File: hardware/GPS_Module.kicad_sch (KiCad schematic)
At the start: 10 parts, among them J3 Conn_01x04_Pin, J4 Conn_01x04_Pin, U6 SAM-M8Q

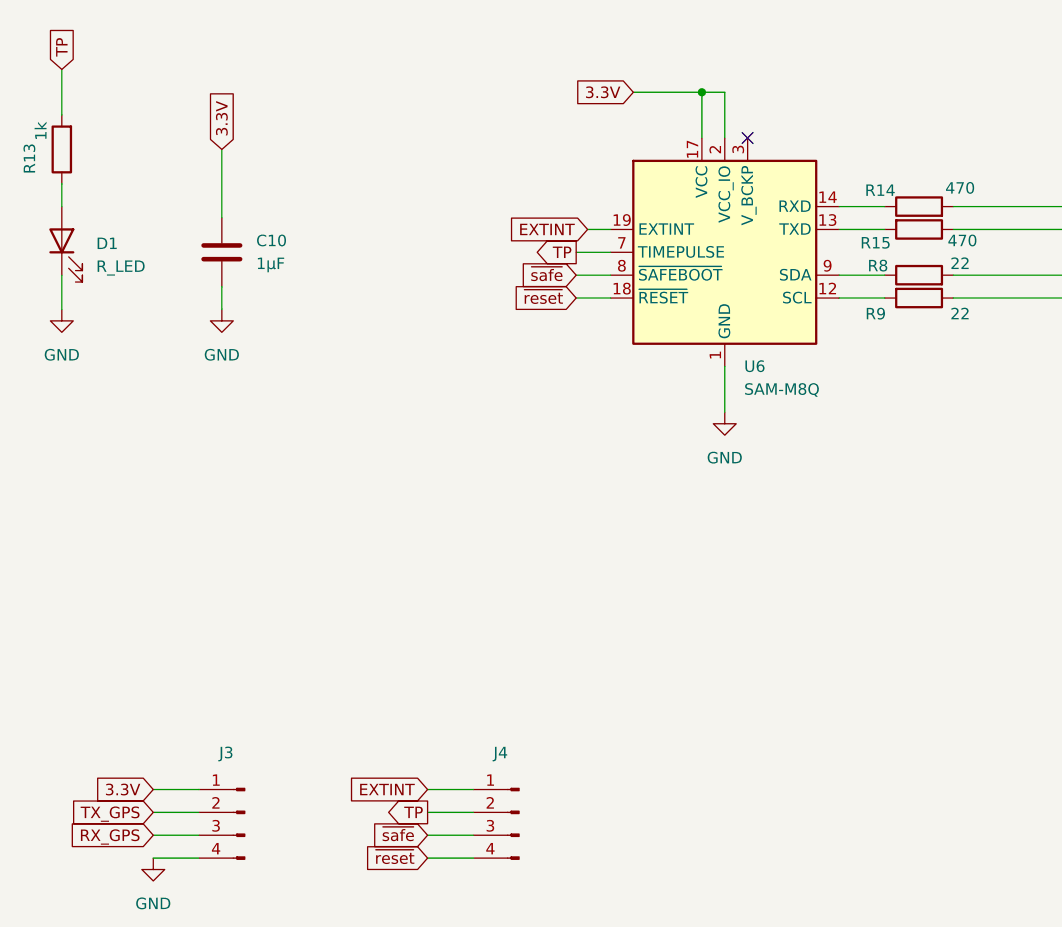
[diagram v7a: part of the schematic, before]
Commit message: Fix schematic components annotations
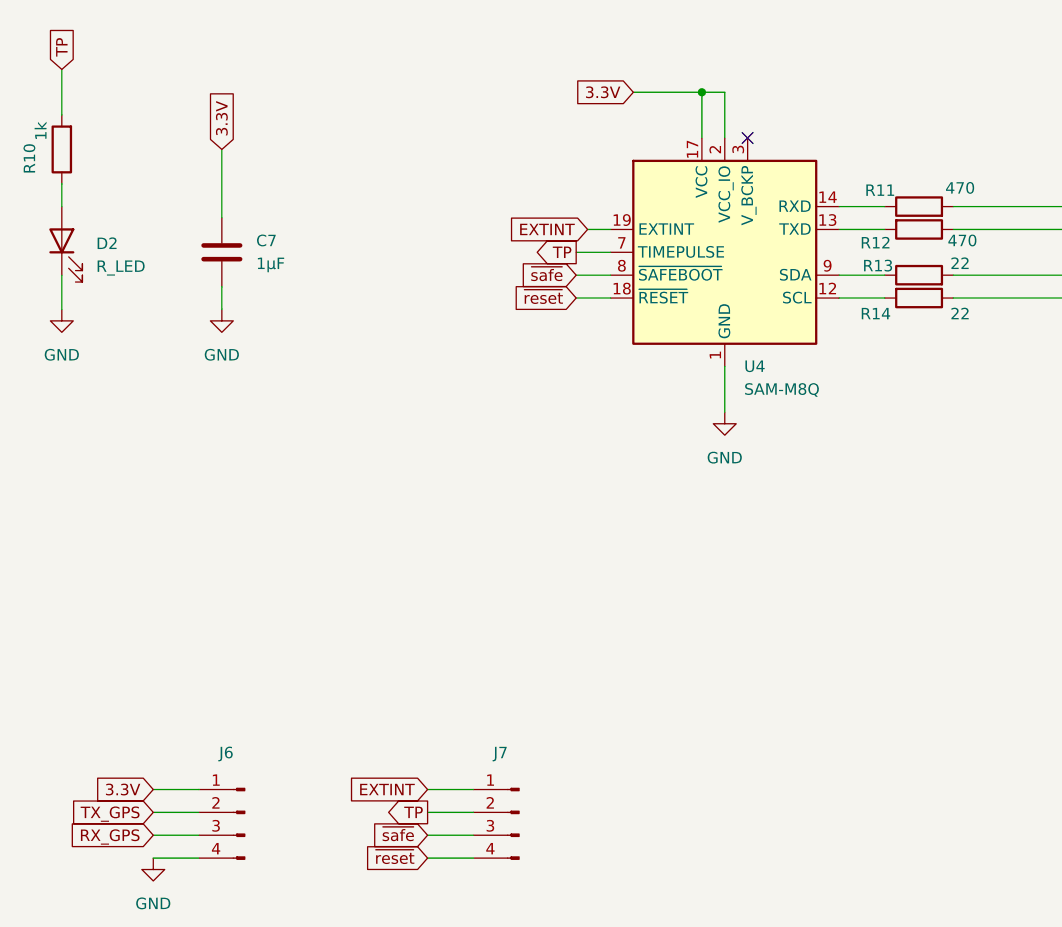
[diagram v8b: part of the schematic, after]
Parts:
- renumbered C10 to C7, D1 to D2, J3 to J6, J4 to J7, R13 to R10, R14 to R11, R15 to R12, R8 to R13, R9 to R14, U6 to U4
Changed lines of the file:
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@@
 		(on_board yes)
 		(dnp no)
-		(property "Reference" "R14"
+		(property "Reference" "R11"
 			(at 169.672 75.692 90)
 			(effects
@@
 			(project "GOG"
 				(path "/5b969f6e-a36e-432b-8f00-b2d6a515a877/86749ea3-b799-4cf0-94d1-46de6ccb32b0"
-					(reference "R14")
+					(reference "R11")
 					(unit 1)
 				)
@@
 		(dnp no)
 		(fields_autoplaced yes)
-		(property "Reference" "#PWR020"
+		(property "Reference" "#PWR019"
 			(at 88.9 156.21 0)
 			(effects
@@
 			(project "GOG"
 				(path "/5b969f6e-a36e-432b-8f00-b2d6a515a877/86749ea3-b799-4cf0-94d1-46de6ccb32b0"
-					(reference "#PWR020")
+					(reference "#PWR019")
 					(unit 1)
 				)
@@
 		(on_board yes)
 		(dnp no)
-		(property "Reference" "R9"
+		(property "Reference" "R14"
 			(at 169.164 89.408 90)
 			(effects
@@
 			(project "GOG"
 				(path "/5b969f6e-a36e-432b-8f00-b2d6a515a877/86749ea3-b799-4cf0-94d1-46de6ccb32b0"
-					(reference "R9")
+					(reference "R14")
 					(unit 1)
 				)
@@
 		(on_board yes)
 		(dnp no)
-		(property "Reference" "R15"
+		(property "Reference" "R12"
 			(at 169.164 81.534 90)
 			(effects
@@
 			(project "GOG"
 				(path "/5b969f6e-a36e-432b-8f00-b2d6a515a877/86749ea3-b799-4cf0-94d1-46de6ccb32b0"
-					(reference "R15")
+					(reference "R12")
 					(unit 1)
 				)
@@
 		(on_board yes)
 		(dnp no)
-		(property "Reference" "R13"
+		(property "Reference" "R10"
 			(at 75.184 72.136 90)
 			(effects
@@
 			(project "GOG"
 				(path "/5b969f6e-a36e-432b-8f00-b2d6a515a877/86749ea3-b799-4cf0-94d1-46de6ccb32b0"
-					(reference "R13")
+					(reference "R10")
 					(unit 1)
 				)
@@
 		(on_board yes)
 		(dnp no)
-		(property "Reference" "R8"
+		(property "Reference" "R13"
 			(at 169.418 84.074 90)
 			(effects
@@
 			(project "GOG"
 				(path "/5b969f6e-a36e-432b-8f00-b2d6a515a877/86749ea3-b799-4cf0-94d1-46de6ccb32b0"
-					(reference "R8")
+					(reference "R13")
 					(unit 1)
 				)
@@
 		(on_board yes)
 		(dnp no)
-		(property "Reference" "J3"
+		(property "Reference" "J6"
 			(at 97.028 138.176 0)
 			(effects
@@
 			(project "GOG"
 				(path "/5b969f6e-a36e-432b-8f00-b2d6a515a877/86749ea3-b799-4cf0-94d1-46de6ccb32b0"
-					(reference "J3")
+					(reference "J6")
 					(unit 1)
 				)
@@
 		(dnp no)
 		(fields_autoplaced yes)
-		(property "Reference" "D1"
+		(property "Reference" "D2"
 			(at 82.55 81.5974 90)
 			(effects
@@
 			(project "GOG"
 				(path "/5b969f6e-a36e-432b-8f00-b2d6a515a877/86749ea3-b799-4cf0-94d1-46de6ccb32b0"
-					(reference "D1")
+					(reference "D2")
 					(unit 1)
 				)
@@
 		(on_board yes)
 		(dnp no)
-		(property "Reference" "J4"
+		(property "Reference" "J7"
 			(at 127.508 138.176 0)
 			(effects
@@
 			(project "GOG"
 				(path "/5b969f6e-a36e-432b-8f00-b2d6a515a877/86749ea3-b799-4cf0-94d1-46de6ccb32b0"
-					(reference "J4")
+					(reference "J7")
 					(unit 1)
 				)
@@
 		(dnp no)
 		(fields_autoplaced yes)
-		(property "Reference" "U6"
+		(property "Reference" "U4"
 			(at 154.5433 95.25 0)
 			(effects
@@
 			(project ""
 				(path "/5b969f6e-a36e-432b-8f00-b2d6a515a877/86749ea3-b799-4cf0-94d1-46de6ccb32b0"
-					(reference "U6")
+					(reference "U4")
 					(unit 1)
 				)
@@
 		(dnp no)
 		(fields_autoplaced yes)
-		(property "Reference" "C10"
+		(property "Reference" "C7"
 			(at 100.33 81.2799 0)
 			(effects
@@
 			(project "GOG"
 				(path "/5b969f6e-a36e-432b-8f00-b2d6a515a877/86749ea3-b799-4cf0-94d1-46de6ccb32b0"
-					(reference "C10")
+					(reference "C7")
 					(unit 1)
 				)
@@
 		(dnp no)
 		(fields_autoplaced yes)
-		(property "Reference" "#PWR018"
+		(property "Reference" "#PWR016"
 			(at 78.74 95.25 0)
 			(effects
@@
 			(project "GOG"
 				(path "/5b969f6e-a36e-432b-8f00-b2d6a515a877/86749ea3-b799-4cf0-94d1-46de6ccb32b0"
-					(reference "#PWR018")
+					(reference "#PWR016")
 					(unit 1)
 				)
@@
 		(dnp no)
 		(fields_autoplaced yes)
-		(property "Reference" "#PWR09"
+		(property "Reference" "#PWR018"
 			(at 152.4 106.68 0)
 			(effects
@@
 			(project ""
 				(path "/5b969f6e-a36e-432b-8f00-b2d6a515a877/86749ea3-b799-4cf0-94d1-46de6ccb32b0"
-					(reference "#PWR09")
-					(unit 1)
-				)
+					(reference "#PWR018")
+					(unit 1)
+				)
